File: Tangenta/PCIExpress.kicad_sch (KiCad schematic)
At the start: 0 parts

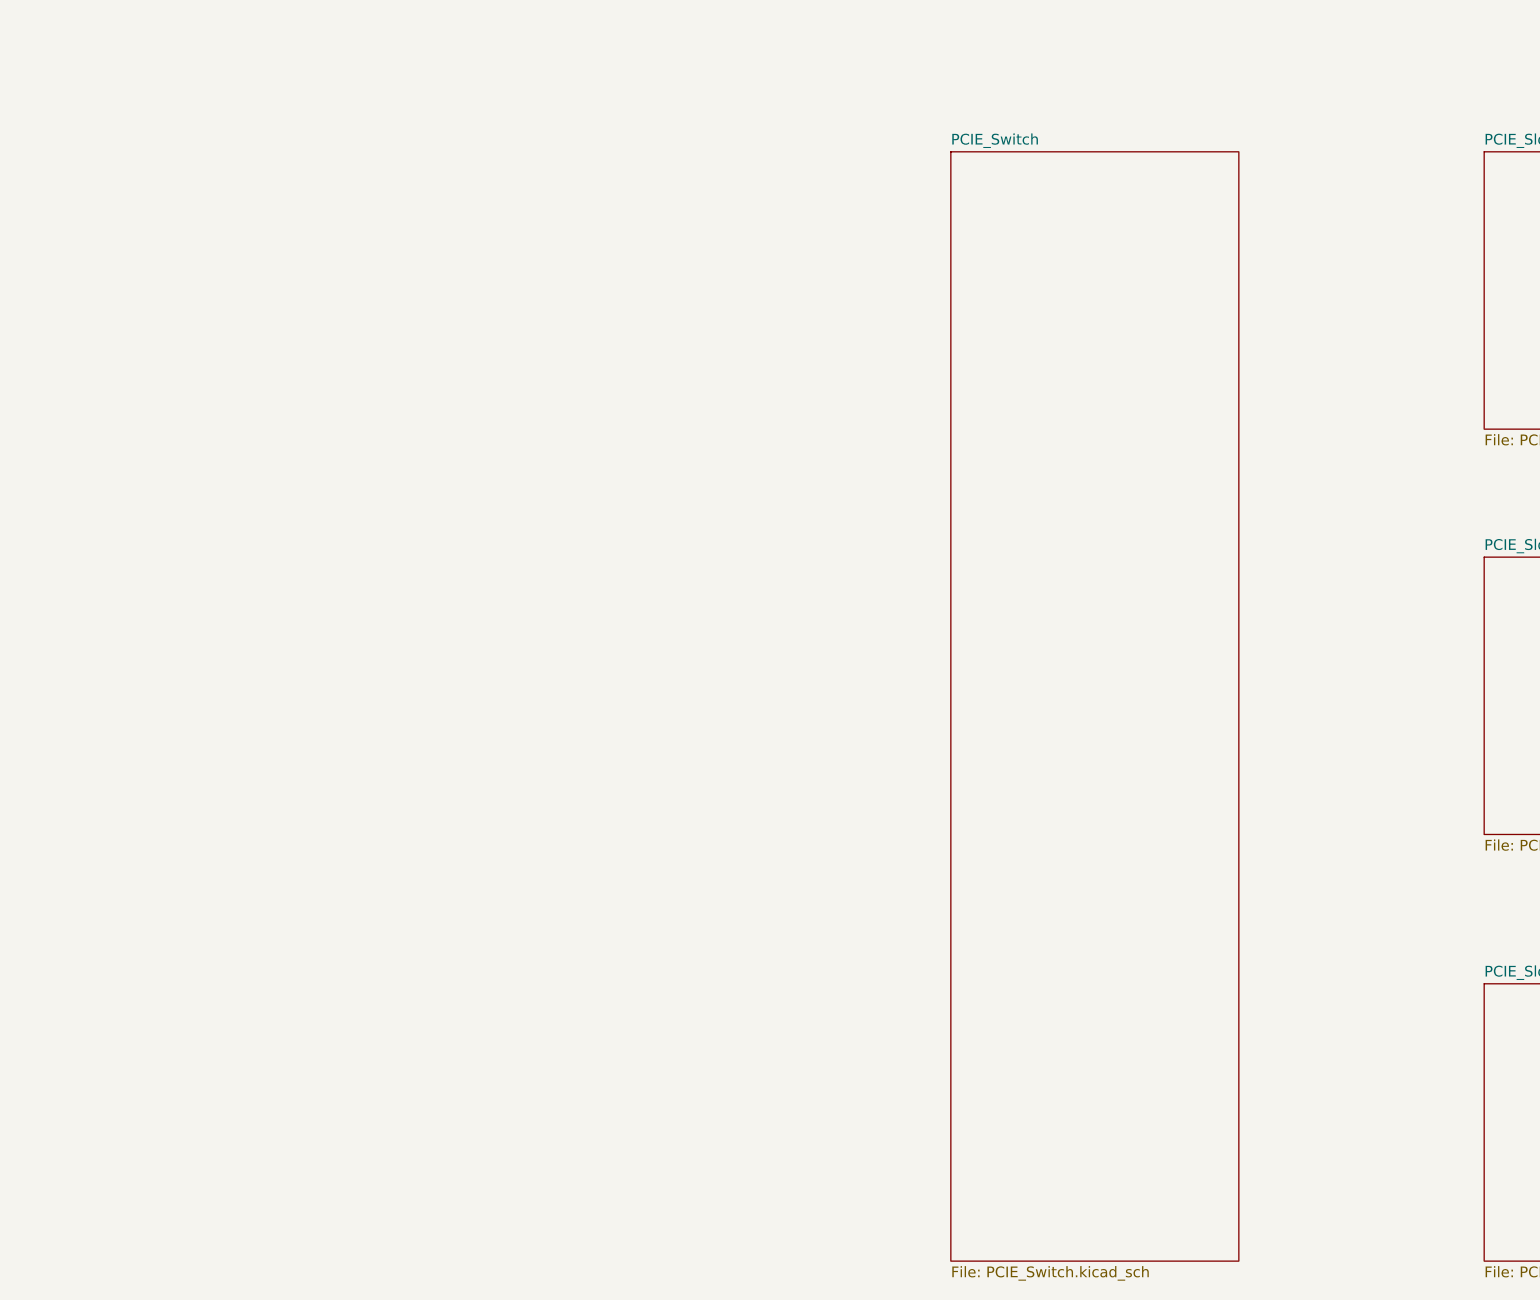
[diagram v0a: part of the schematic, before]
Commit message: PCIe current progress, hierarchy
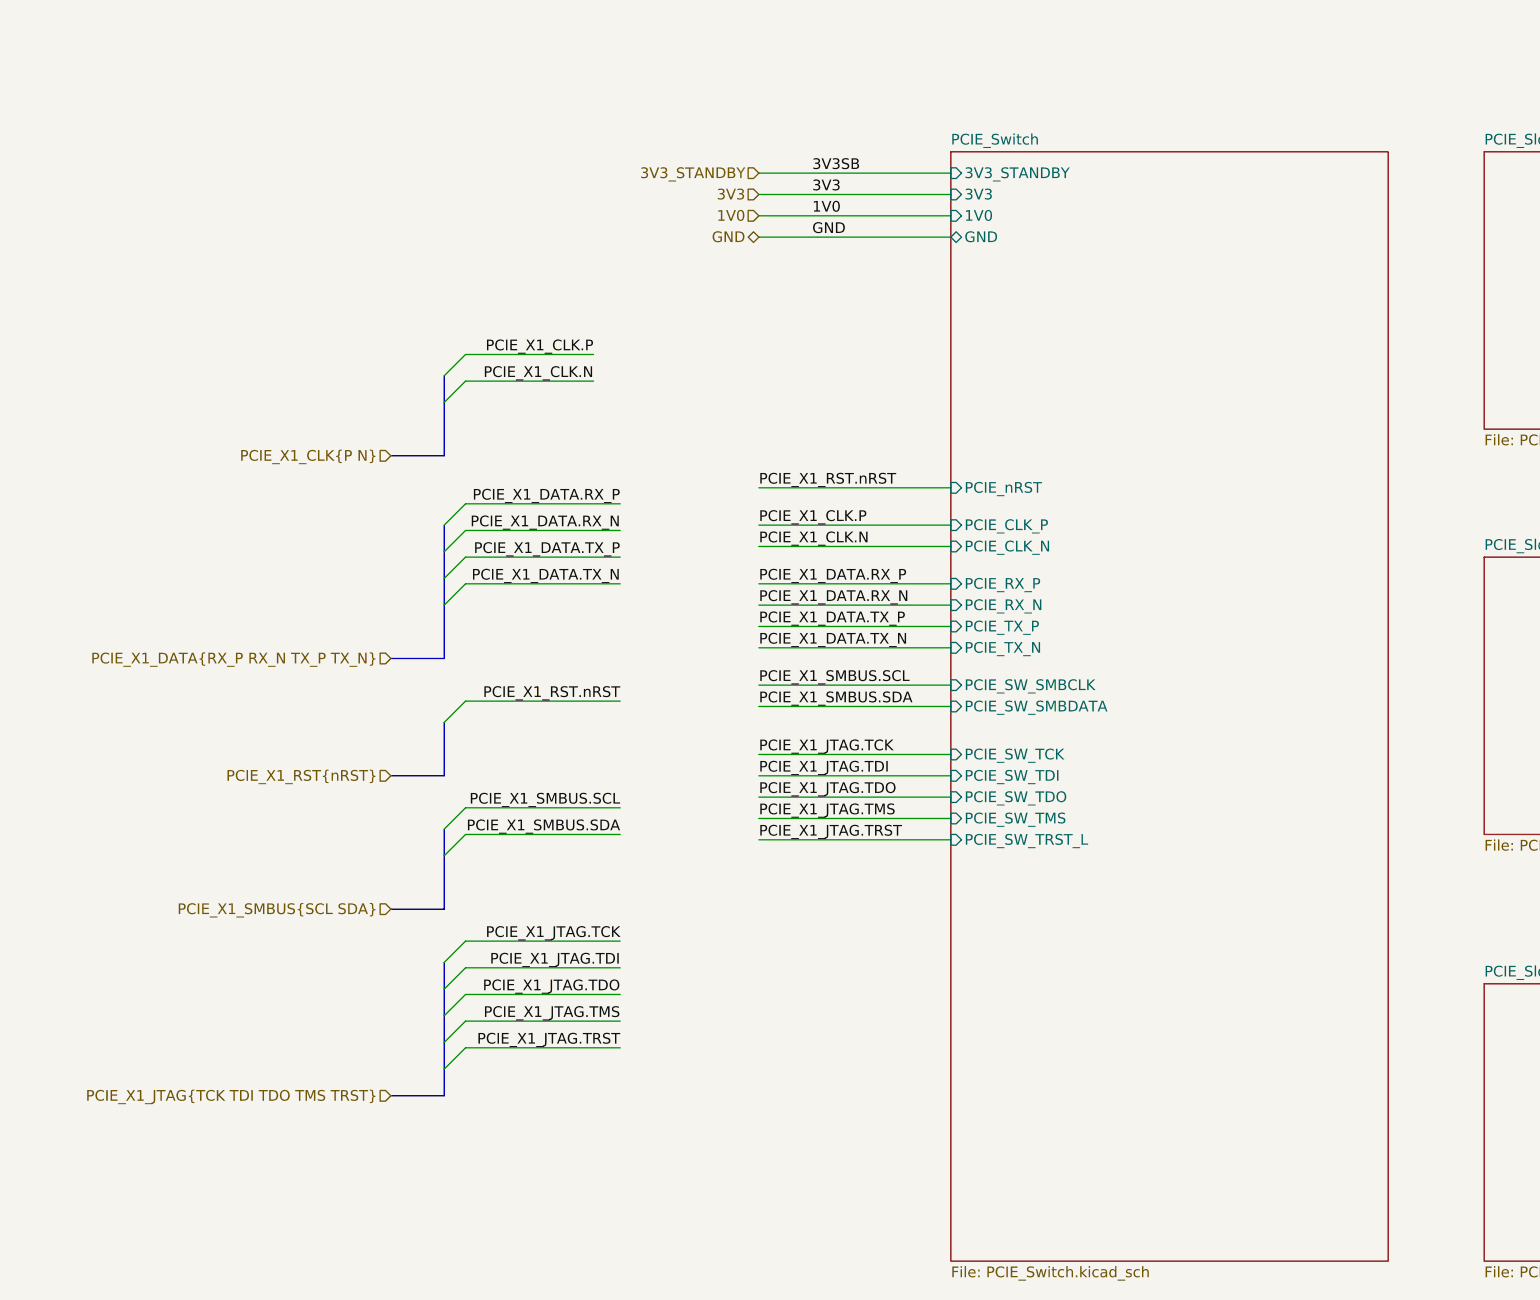
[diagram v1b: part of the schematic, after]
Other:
- sheet PCIE_Switch ports: added 1V0, 3V3, 3V3_STANDBY, GND, PCIE_CLK_N, PCIE_CLK_P, PCIE_RX_N, PCIE_RX_P, PCIE_SW_SMBCLK, PCIE_SW_SMBDATA, PCIE_SW_TCK, PCIE_SW_TDI, PCIE_SW_TDO, PCIE_SW_TMS, PCIE_SW_TRST_L, PCIE_TX_N, PCIE_TX_P, PCIE_nRST; removed none

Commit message: PCIe current progress.
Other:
- sheet PCIE_Switch ports: added 1V0_STANDBY; removed none
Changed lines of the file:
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@@
+    (stroke (width 0) (type default))
+  )
+  (wire (pts (xy 124.46 76.2) (xy 101.6 76.2))
     (stroke (width 0) (type default))
   )
@@
     (stroke (width 0) (type default))
   )
-  (wire (pts (xy 124.46 76.2) (xy 101.6 76.2))
+  (wire (pts (xy 124.46 78.74) (xy 101.6 78.74))
     (stroke (width 0) (type default))
   )
@@
     (effects (font (size 1.27 1.27)) (justify right bottom))
   )
+  (label "1V0SB" (at 107.95 76.2 0) (fields_autoplaced)
+    (effects (font (size 1.27 1.27)) (justify left bottom))
+  )
   (label "PCIE_X1_JTAG.TRST" (at 85.09 172.72 180) (fields_autoplaced)
     (effects (font (size 1.27 1.27)) (justify right bottom))
@@
     (effects (font (size 1.27 1.27)) (justify left bottom))
   )
-  (label "GND" (at 107.95 76.2 0) (fields_autoplaced)
+  (label "GND" (at 107.95 78.74 0) (fields_autoplaced)
     (effects (font (size 1.27 1.27)) (justify left bottom))
   )
@@
     (effects (font (size 1.27 1.27)) (justify right))
   )
-  (hierarchical_label "GND" (shape bidirectional) (at 101.6 76.2 180) (fields_autoplaced)
+  (hierarchical_label "GND" (shape bidirectional) (at 101.6 78.74 180) (fields_autoplaced)
     (effects (font (size 1.27 1.27)) (justify right))
   )
   (hierarchical_label "PCIE_X1_JTAG{TCK TDI TDO TMS TRST}" (shape input) (at 57.785 178.435 180) (fields_autoplaced)
+    (effects (font (size 1.27 1.27)) (justify right))
+  )
+  (hierarchical_label "1V0_STANDBY" (shape input) (at 101.6 76.2 180) (fields_autoplaced)
     (effects (font (size 1.27 1.27)) (justify right))
   )
@@
       (effects (font (size 1.27 1.27)) (justify left))
     )
-    (pin "GND" bidirectional (at 124.46 76.2 180)
+    (pin "GND" bidirectional (at 124.46 78.74 180)
       (effects (font (size 1.27 1.27)) (justify left))
     )
@@
       (effects (font (size 1.27 1.27)) (justify left))
     )
+    (pin "1V0_STANDBY" input (at 124.46 76.2 180)
+      (effects (font (size 1.27 1.27)) (justify left))
+    )

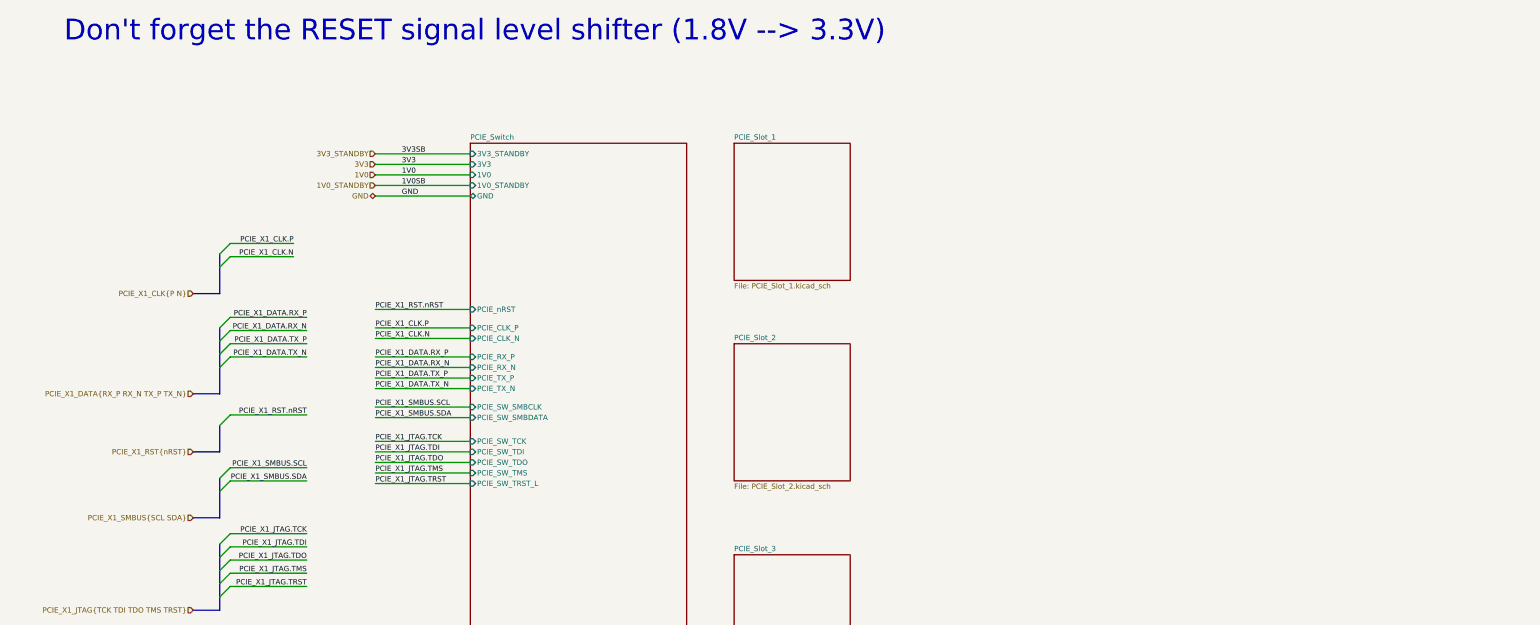
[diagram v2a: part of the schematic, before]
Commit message: PCIe nWAKE signal...
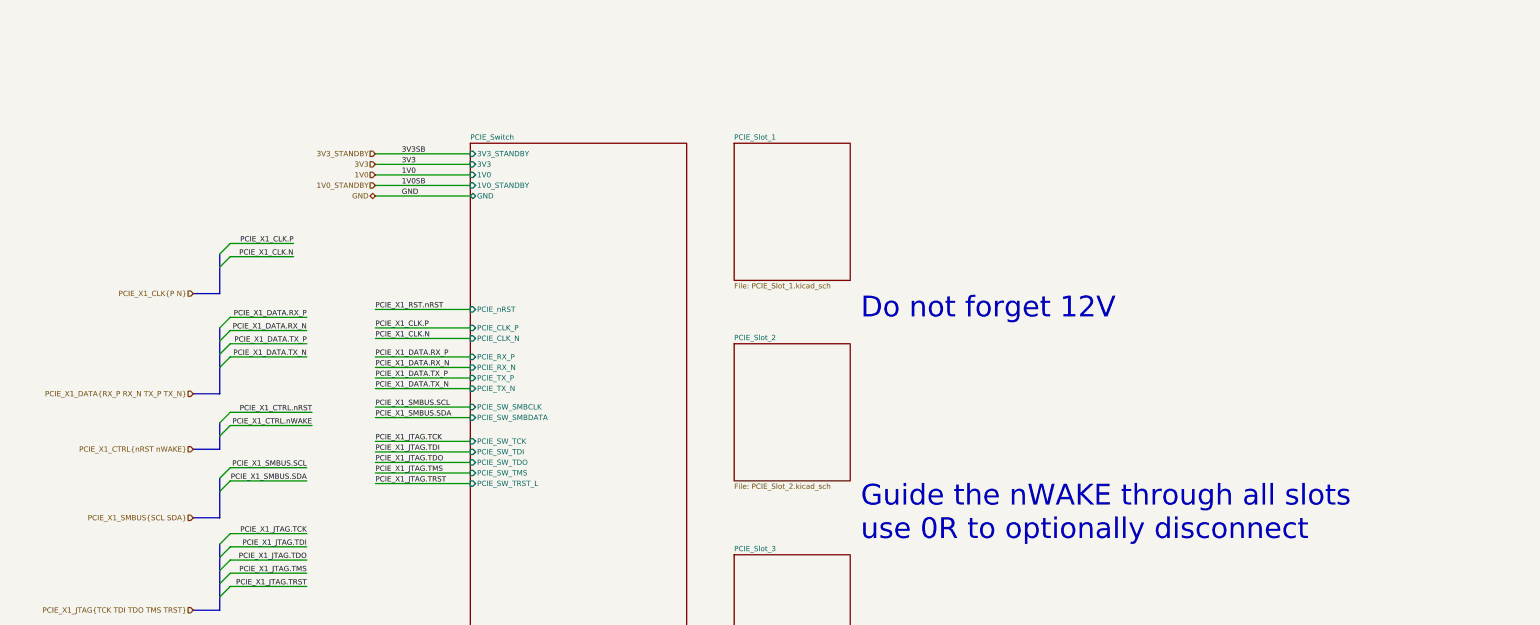
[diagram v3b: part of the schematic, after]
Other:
- note added: "Do not forget 12V"
- note added: "Guide the nWAKE through all slots use 0R to optionally disconnect"
- note removed: "Don't forget the RESET signal level shifter (1.8V --> 3.3V)"
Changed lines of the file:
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@@
+    (stroke (width 0) (type default))
+  )
+  (bus_entry (at 64.135 136.525) (size 2.54 -2.54)
     (stroke (width 0) (type default))
   )
@@
     (stroke (width 0) (type default))
   )
+  (bus_entry (at 64.135 133.35) (size 2.54 -2.54)
+    (stroke (width 0) (type default))
+  )
   (bus_entry (at 64.135 95.885) (size 2.54 -2.54)
     (stroke (width 0) (type default))
   )
-  (bus_entry (at 64.135 133.985) (size 2.54 -2.54)
-    (stroke (width 0) (type default))
-  )
   (bus_entry (at 64.135 92.71) (size 2.54 -2.54)
     (stroke (width 0) (type default))
@@
     (stroke (width 0) (type default))
   )
-  (bus (pts (xy 64.135 133.985) (xy 64.135 140.335))
-    (stroke (width 0) (type default))
-  )
   (wire (pts (xy 101.6 147.955) (xy 124.46 147.955))
     (stroke (width 0) (type default))
@@
     (stroke (width 0) (type default))
   )
+  (bus (pts (xy 64.135 133.35) (xy 64.135 136.525))
+    (stroke (width 0) (type default))
+  )
   (wire (pts (xy 101.6 142.875) (xy 124.46 142.875))
     (stroke (width 0) (type default))
@@
     (stroke (width 0) (type default))
   )
-  (wire (pts (xy 66.675 131.445) (xy 85.09 131.445))
-    (stroke (width 0) (type default))
-  )
   (wire (pts (xy 101.6 132.08) (xy 124.46 132.08))
     (stroke (width 0) (type default))
@@
     (stroke (width 0) (type default))
   )
+  (bus (pts (xy 57.785 139.7) (xy 64.135 139.7))
+    (stroke (width 0) (type default))
+  )
   (bus (pts (xy 64.135 120.015) (xy 64.135 126.365))
     (stroke (width 0) (type default))
@@
     (stroke (width 0) (type default))
   )
+  (wire (pts (xy 66.675 133.985) (xy 86.36 133.985))
+    (stroke (width 0) (type default))
+  )
+  (bus (pts (xy 64.135 136.525) (xy 64.135 139.7))
+    (stroke (width 0) (type default))
+  )
   (wire (pts (xy 66.675 114.3) (xy 85.09 114.3))
     (stroke (width 0) (type default))
@@
     (stroke (width 0) (type default))
   )
-  (bus (pts (xy 57.785 140.335) (xy 64.135 140.335))
+  (wire (pts (xy 66.675 130.81) (xy 86.36 130.81))
     (stroke (width 0) (type default))
   )
@@
     (stroke (width 0) (type default))
   )
-  (text "Don't forget the RESET signal level shifter (1.8V --> 3.3V)"
-    (at 26.67 41.91 0)
+  (text "Guide the nWAKE through all slots\nuse 0R to optionally disconnect"
+    (at 218.44 161.925 0)
     (effects (font (size 5 5)) (justify left bottom))
   )
-  (label "PCIE_X1_RST.nRST" (at 85.09 131.445 180) (fields_autoplaced)
-    (effects (font (size 1.27 1.27)) (justify right bottom))
+  (text "Do not forget 12V" (at 218.44 108.585 0)
+    (effects (font (size 5 5)) (justify left bottom))
   )
   (label "PCIE_X1_CLK.P" (at 81.915 90.17 180) (fields_autoplaced)
@@
     (effects (font (size 1.27 1.27)) (justify left bottom))
   )
+  (label "PCIE_X1_CTRL.nRST" (at 86.36 130.81 180) (fields_autoplaced)
+    (effects (font (size 1.27 1.27)) (justify right bottom))
+  )
   (label "PCIE_X1_JTAG.TMS" (at 85.09 169.545 180) (fields_autoplaced)
     (effects (font (size 1.27 1.27)) (justify right bottom))
@@
     (effects (font (size 1.27 1.27)) (justify left bottom))
   )
+  (label "PCIE_X1_CTRL.nWAKE" (at 86.36 133.985 180) (fields_autoplaced)
+    (effects (font (size 1.27 1.27)) (justify right bottom))
+  )
   (label "PCIE_X1_RST.nRST" (at 101.6 106.045 0) (fields_autoplaced)
     (effects (font (size 1.27 1.27)) (justify left bottom))
@@
   (label "PCIE_X1_CLK.N" (at 81.915 93.345 180) (fields_autoplaced)
     (effects (font (size 1.27 1.27)) (justify right bottom))
-  )
-  (hierarchical_label "PCIE_X1_RST{nRST}" (shape input) (at 57.785 140.335 180) (fields_autoplaced)
-    (effects (font (size 1.27 1.27)) (justify right))
   )
   (hierarchical_label "3V3" (shape input) (at 101.6 71.12 180) (fields_autoplaced)
@@
     (effects (font (size 1.27 1.27)) (justify right))
   )
+  (hierarchical_label "PCIE_X1_CTRL{nRST nWAKE}" (shape input) (at 57.785 139.7 180) (fields_autoplaced)
+    (effects (font (size 1.27 1.27)) (justify right))
+  )

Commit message: PCIe schematic continued...
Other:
- sheet PCIE_Slot_1 ports: added PCIE1_CLK_N, PCIE1_CLK_P, PCIE1_PERST, PCIE1_PRSNT, PCIE1_RX_N, PCIE1_RX_P, PCIE1_TX_N, PCIE1_TX_P; removed none
- sheet PCIE_Slot_2 ports: added PCIE2_CLK_N, PCIE2_CLK_P, PCIE2_PERST, PCIE2_PRSNT, PCIE2_RX_N, PCIE2_RX_P, PCIE2_TX_N, PCIE2_TX_P; removed none
- sheet PCIE_Slot_3 ports: added PCIE3_CLK_N, PCIE3_CLK_P, PCIE3_PERST, PCIE3_PRSNT, PCIE3_RX_N, PCIE3_RX_P, PCIE3_TX_N, PCIE3_TX_P; removed none
- sheet PCIE_Switch ports: added PCIE1_CLK_N, PCIE1_CLK_P, PCIE1_PERST, PCIE1_PRSNT, PCIE1_RX_N, PCIE1_RX_P, PCIE1_TX_N, PCIE1_TX_P, PCIE2_CLK_N, PCIE2_CLK_P, PCIE2_PERST, PCIE2_PRSNT, PCIE2_RX_N, PCIE2_RX_P, PCIE2_TX_N, PCIE2_TX_P, PCIE3_CLK_N, PCIE3_CLK_P, PCIE3_PERST, PCIE3_PRSNT, PCIE3_RX_N, PCIE3_RX_P, PCIE3_TX_N, PCIE3_TX_P; removed none
